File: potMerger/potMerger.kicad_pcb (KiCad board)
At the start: 2 copper layers, 10 x 9 mm, 3 parts, among them J1 Conn_01x04_Female, J2 Conn_01x03_Female, J3 Conn_01x03_Female

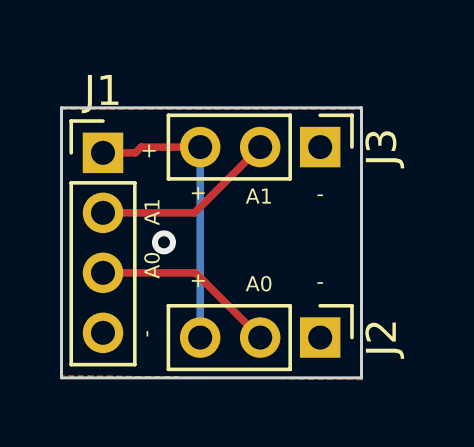
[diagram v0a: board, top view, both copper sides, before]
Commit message: potMerger : made it 0.25 mm wider
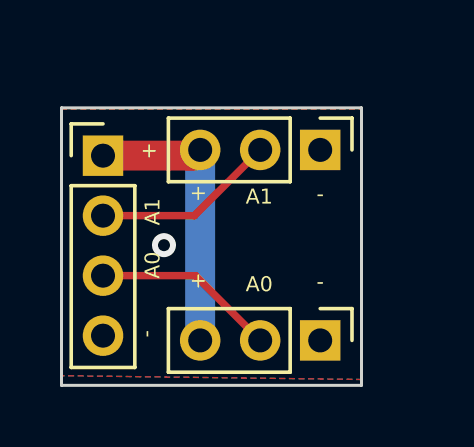
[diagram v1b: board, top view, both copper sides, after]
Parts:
- moved J1 0.09 mm to (151.4, 51.6)
- moved J2 0.09 mm to (158.6, 57.8)
- moved J3 0.09 mm to (158.6, 51.4)
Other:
- board size 10 x 9 mm -> 10 x 9.2 mm
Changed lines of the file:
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@@
   (net 4 "GND")
   (footprint "Connector_PinHeader_2.00mm:PinHeader_1x04_P2.00mm_Vertical" (layer "F.Cu")
-    (at 151.384 51.5)
+    (at 151.384 51.594)
     (descr "Through hole straight pin header, 1x04, 2.00mm pitch, single row")
     (tags "Through hole pin header THT 1x04 2.00mm single row")
@@
     (property "Sheetname" "")
     (attr through_hole)
-    (fp_text reference "J1" (at 0 -2.06) (layer "F.SilkS")
+    (fp_text reference "J1" (at 0 -2.06) (layer "F.SilkS") hide
       (effects (font (size 1 1) (thickness 0.15)))
     )
@@
   )
   (footprint "Connector_PinHeader_2.00mm:PinHeader_1x03_P2.00mm_Vertical" (layer "F.Cu")
-    (at 158.623 51.308 -90)
+    (at 158.623 51.402 -90)
     (descr "Through hole straight pin header, 1x03, 2.00mm pitch, single row")
     (tags "Through hole pin header THT 1x03 2.00mm single row")
@@
     (property "Sheetname" "")
     (attr through_hole)
-    (fp_text reference "J3" (at 0 -2.06 90) (layer "F.SilkS")
+    (fp_text reference "J3" (at 0 -2.06 90) (layer "F.SilkS") hide
       (effects (font (size 1 1) (thickness 0.15)))
     )
@@
   )
   (footprint "Connector_PinHeader_2.00mm:PinHeader_1x03_P2.00mm_Vertical" (layer "F.Cu")
-    (at 158.623 57.658 -90)
+    (at 158.623 57.752 -90)
     (descr "Through hole straight pin header, 1x03, 2.00mm pitch, single row")
     (tags "Through hole pin header THT 1x03 2.00mm single row")
@@
     (property "Sheetname" "")
     (attr through_hole)
-    (fp_text reference "J2" (at 0 -2.06 90) (layer "F.SilkS")
+    (fp_text reference "J2" (at 0 -2.06 90) (layer "F.SilkS") hide
       (effects (font (size 1 1) (thickness 0.15)))
     )
@@
       (net 1 "+3.3V") (pinfunction "Pin_3") (pintype "passive"))
   )
-  (gr_rect (start 150 50) (end 160 59) (layer "Edge.Cuts") (width 0.1) (fill none))
+  (gr_rect (start 150 50) (end 160 59.25) (layer "Edge.Cuts") (width 0.1) (fill none))
   (gr_text "+" (at 154.559 55.753) (layer "F.SilkS")
     (effects (font (size 0.5 0.5) (thickness 0.1)))
@@
   )
   (dimension (type aligned) (layer "Margin")
-    (pts (xy 160 59) (xy 150 59))
-    (height -5)
-    (gr_text "10,0000 mm" (at 155 62.85) (layer "Margin")
+    (pts (xy 150 50) (xy 160 50))
+    (height -7)
+    (gr_text "10.0000 mm" (at 155 41.85) (layer "Margin")
       (effects (font (size 1 1) (thickness 0.15)))
     )
@@
   )
   (dimension (type aligned) (layer "Margin")
-    (pts (xy 150 50) (xy 160 50))
-    (height -7)
-    (gr_text "10,0000 mm" (at 155 41.85) (layer "Margin")
+    (pts (xy 150 50) (xy 150 59.25))
+    (height 4.585)
+    (gr_text "9.2500 mm" (at 144.265 54.625 90) (layer "Margin")
       (effects (font (size 1 1) (thickness 0.15)))
     )
@@
     (style (thickness 0.15) (arrow_length 1.27) (text_position_mode 0) (extension_height 0.58642) (extension_offset 0.5) keep_text_aligned)
   )
-  (dimension (type aligned) (layer "Margin")
-    (pts (xy 160 50) (xy 160 59))
-    (height -6)
-    (gr_text "9,0000 mm" (at 164.85 54.5 90) (layer "Margin")
-      (effects (font (size 1 1) (thickness 0.15)))
-    )
-    (format (units 3) (units_format 1) (precision 4))
-    (style (thickness 0.15) (arrow_length 1.27) (text_position_mode 0) (extension_height 0.58642) (extension_offset 0.5) keep_text_aligned)
-  )
-  (dimension (type aligned) (layer "Margin")
-    (pts (xy 150 59) (xy 150 50))
-    (height -6)
-    (gr_text "9,0000 mm" (at 142.85 54.5 90) (layer "Margin")
-      (effects (font (size 1 1) (thickness 0.15)))
-    )
-    (format (units 3) (units_format 1) (precision 4))
-    (style (thickness 0.15) (arrow_length 1.27) (text_position_mode 0) (extension_height 0.58642) (extension_offset 0.5) keep_text_aligned)
-  )
-  (segment (start 152.465 51.5) (end 152.657 51.308) (width 0.25) (layer "F.Cu") (net 1))
-  (segment (start 151.384 51.5) (end 152.465 51.5) (width 0.25) (layer "F.Cu") (net 1))
-  (segment (start 152.657 51.308) (end 154.623 51.308) (width 0.25) (layer "F.Cu") (net 1))
-  (segment (start 154.623 57.658) (end 154.623 51.308) (width 0.25) (layer "B.Cu") (net 1))
-  (segment (start 154.431 53.5) (end 156.623 51.308) (width 0.25) (layer "F.Cu") (net 2))
-  (segment (start 151.384 53.5) (end 154.431 53.5) (width 0.25) (layer "F.Cu") (net 2))
-  (segment (start 151.384 55.5) (end 154.465 55.5) (width 0.25) (layer "F.Cu") (net 3))
-  (segment (start 154.465 55.5) (end 156.623 57.658) (width 0.25) (layer "F.Cu") (net 3))
-  (via (at 153.416 54.483) (size 0.8) (drill 0.4) (layers "F.Cu" "B.Cu") (free) (net 4))
+  (segment (start 151.384 51.594) (end 154.431 51.594) (width 1) (layer "F.Cu") (net 1))
+  (segment (start 154.431 51.5) (end 154.623 51.308) (width 1) (layer "F.Cu") (net 1))
+  (segment (start 154.623 51.402) (end 154.623 57.752) (width 1) (layer "B.Cu") (net 1))
+  (segment (start 154.431 53.594) (end 156.623 51.402) (width 0.25) (layer "F.Cu") (net 2))
+  (segment (start 151.384 53.594) (end 154.431 53.594) (width 0.25) (layer "F.Cu") (net 2))
+  (segment (start 151.384 55.594) (end 154.465 55.594) (width 0.25) (layer "F.Cu") (net 3))
+  (segment (start 154.465 55.594) (end 156.623 57.752) (width 0.25) (layer "F.Cu") (net 3))
+  (via (at 153.416 54.577) (size 0.8) (drill 0.4) (layers "F.Cu" "B.Cu") (free) (net 4))
   (zone (net 4) (net_name "GND") (layers F&B.Cu) (hatch edge 0.508)
     (connect_pads (clearance 0.508))
